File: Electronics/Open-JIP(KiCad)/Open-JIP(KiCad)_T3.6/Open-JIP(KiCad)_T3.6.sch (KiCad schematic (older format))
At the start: 31 parts, among them J1 EJ503A, J2 Screw_Terminal_01x02, U1 74HC4066D,653, U2 74HC4066D,653, U3 KA7812ETU, U4 OPA320AIDBVT, U5 Teensy3.6

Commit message: finished v0.3 for teensy 3.2 and added gerber files
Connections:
- net GNDA: now also C5.2, U4.2 (V-)
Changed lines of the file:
@@
 	1950 5250 1950 5350
 Connection ~ 1950 5350
+Wire Wire Line
+	4300 3800 4300 4100
+Wire Wire Line
+	4300 4100 4450 4100
+Connection ~ 4300 3800
+Connection ~ 4450 4100
 $EndSCHEMATC

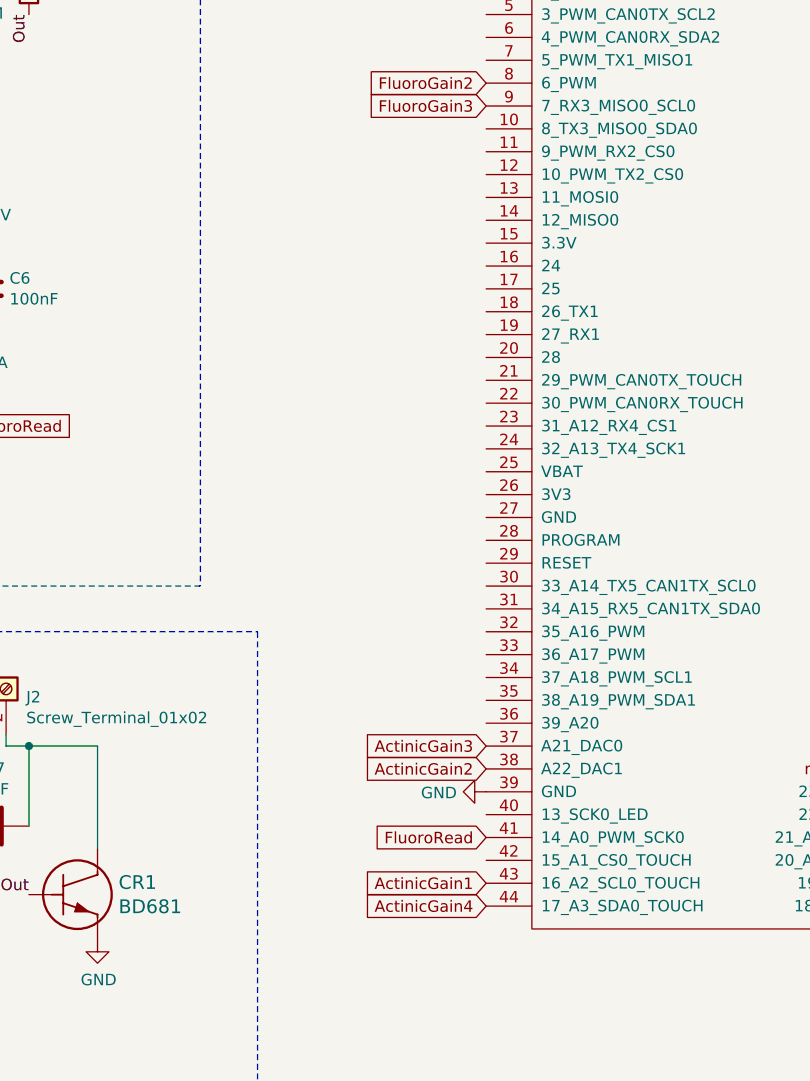
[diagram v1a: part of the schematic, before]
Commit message: added J-step measuring procedure
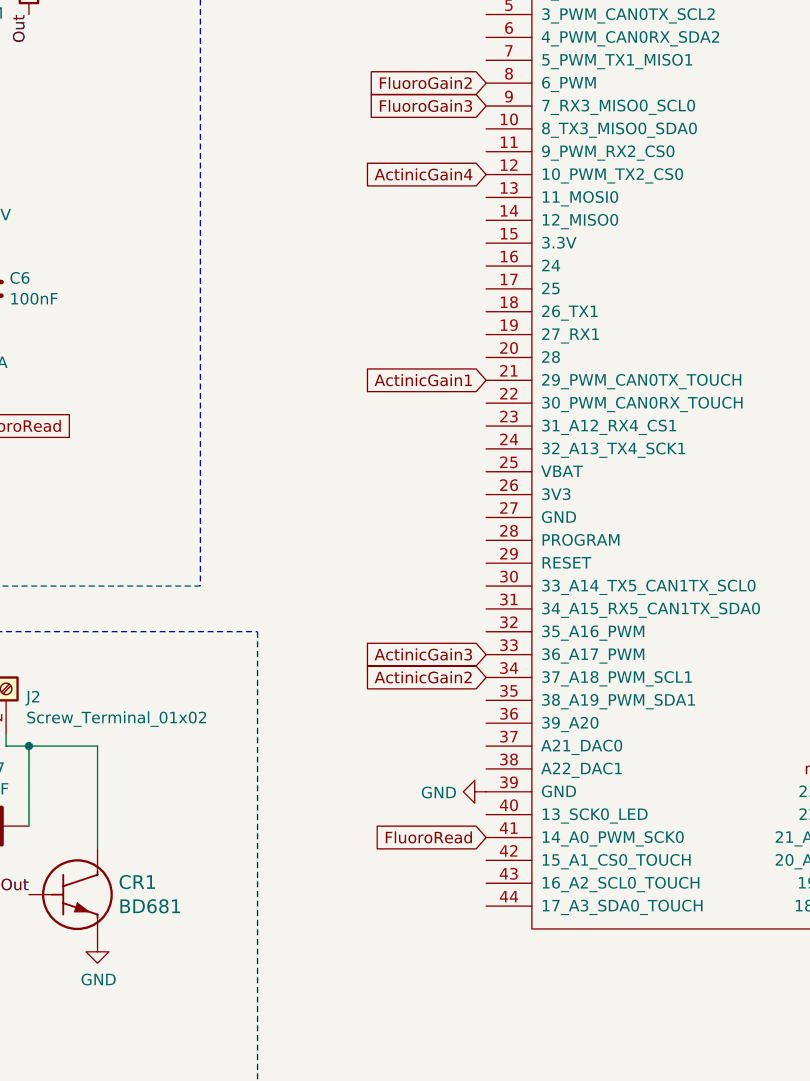
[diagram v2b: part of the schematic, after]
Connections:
- net ActinicGain1: now also U5.21 (29_PWM_CAN0TX_TOUCH); no longer U5.43 (16_A2_SCL0_TOUCH)
- net ActinicGain2: now also U5.34 (37_A18_PWM_SCL1); no longer U5.38 (A22_DAC1)
- net ActinicGain3: now also U5.33 (36_A17_PWM); no longer U5.37 (A21_DAC0)
- net ActinicGain4: now also U5.12 (10_PWM_TX2_CS0); no longer U5.44 (17_A3_SDA0_TOUCH)
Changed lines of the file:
@@
 Text GLabel 2500 6700 0    50   Input ~ 0
 ActinicGain4
-Text GLabel 7200 5700 0    50   Input ~ 0
+Text GLabel 7200 3500 0    50   Input ~ 0
 ActinicGain1
-Text GLabel 7200 5200 0    50   Input ~ 0
+Text GLabel 7200 4800 0    50   Input ~ 0
 ActinicGain2
-Text GLabel 7200 5100 0    50   Input ~ 0
+Text GLabel 7200 4700 0    50   Input ~ 0
 ActinicGain3
-Text GLabel 7200 5800 0    50   Input ~ 0
+Text GLabel 7200 2600 0    50   Input ~ 0
 ActinicGain4
 $Comp

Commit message: update firmware for v0.3
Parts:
- R11: value 4.3K -> 5.1K
- R4: value 8.2K -> 10K
- R6: value 6.8K -> 8.2K
- R8: value 2.3M -> 2M
- R9: value 5.1K -> 6.8K
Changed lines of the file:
@@
 P 4850 1850
 F 0 "R8" H 4780 1804 50  0000 R CNN
-F 1 "2.3M" H 4780 1895 50  0000 R CNN
+F 1 "2M" H 4780 1895 50  0000 R CNN
 F 2 "Resistor_SMD:R_0805_2012Metric_Pad1.20x1.40mm_HandSolder" V 4780 1850 50  0001 C CNN
 F 3 "~" H 4850 1850 50  0001 C CNN
@@
 P 4250 7050
 F 0 "R4" H 4180 7004 50  0000 R CNN
-F 1 "8.2K" H 4180 7095 50  0000 R CNN
+F 1 "10K" H 4180 7095 50  0000 R CNN
 F 2 "Resistor_SMD:R_0805_2012Metric_Pad1.20x1.40mm_HandSolder" V 4180 7050 50  0001 C CNN
 F 3 "~" H 4250 7050 50  0001 C CNN
@@
 P 4950 6850
 F 0 "R9" H 4880 6804 50  0000 R CNN
-F 1 "5.1K" H 4880 6895 50  0000 R CNN
+F 1 "6.8K" H 4880 6895 50  0000 R CNN
 F 2 "Resistor_SMD:R_0805_2012Metric_Pad1.20x1.40mm_HandSolder" V 4880 6850 50  0001 C CNN
 F 3 "~" H 4950 6850 50  0001 C CNN
@@
 P 5300 6750
 F 0 "R11" H 5230 6704 50  0000 R CNN
-F 1 "4.3K" H 5230 6795 50  0000 R CNN
+F 1 "5.1K" H 5230 6795 50  0000 R CNN
 F 2 "Resistor_SMD:R_0805_2012Metric_Pad1.20x1.40mm_HandSolder" V 5230 6750 50  0001 C CNN
 F 3 "~" H 5300 6750 50  0001 C CNN
@@
 P 4600 6950
 F 0 "R6" H 4530 6904 50  0000 R CNN
-F 1 "6.8K" H 4530 6995 50  0000 R CNN
+F 1 "8.2K" H 4530 6995 50  0000 R CNN
 F 2 "Resistor_SMD:R_0805_2012Metric_Pad1.20x1.40mm_HandSolder" V 4530 6950 50  0001 C CNN
 F 3 "~" H 4600 6950 50  0001 C CNN

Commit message: adding optical density to fluorometer
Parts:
- removed U3: KA7812ETU, Additional-parts:TO253P1067X470X2040-3, symbol KA7812ETU:KA7812ETU
- added C? (x2): 100nF, Capacitor_SMD:C_0805_2012Metric_Pad1.18x1.45mm_HandSolder, symbol Open-JIP(KiCad)_T3.6-rescue:C-Device
- added D?: LED, symbol Device:LED
- added Q?: FDN337N, SSOT-3, symbol FDN337N:FDN337N
- added R?: 300, Resistor_SMD:R_0805_2012Metric_Pad1.20x1.40mm_HandSolder, symbol Open-JIP(KiCad)_T3.6-rescue:R-Device
- added R?: 50K, Resistor_SMD:R_0805_2012Metric_Pad1.20x1.40mm_HandSolder, symbol Open-JIP(KiCad)_T3.6-rescue:R-Device
- added R?: 220, Resistor_SMD:R_0805_2012Metric_Pad1.20x1.40mm_HandSolder, symbol Open-JIP(KiCad)_T3.6-rescue:R-Device
- added R?: 10K, Resistor_SMD:R_0805_2012Metric_Pad1.20x1.40mm_HandSolder, symbol Open-JIP(KiCad)_T3.6-rescue:R-Device
- added TP?: 0.001, symbol Connector:TestPoint
- added TP?: OA-Out, symbol Connector:TestPoint
- added TP?: FG1, symbol Connector:TestPoint
- added TP?: FG2, symbol Connector:TestPoint
- added TP?: FG3, symbol Connector:TestPoint
- added TP?: FG4, symbol Connector:TestPoint
- added TP? (x2): AGND, symbol Connector:TestPoint
- added TP?: ODPwr, symbol Connector:TestPoint
- added TP?: 12V, symbol Connector:TestPoint
- added TP?: 6V, symbol Connector:TestPoint
- added U?: OPA320AIDBVT, Additional-parts:SOT95P280X145-5N, symbol Open-JIP(KiCad)_T3.6-rescue:OPA320AIDBVT-OPA320AIDBVT
- added U?: L7806CD2T-TR, symbol VREG_L7806CD2T-TR:L7806CD2T-TR
- C1, C2, C3, C4, C5, C6: symbol Device:C -> Open-JIP(KiCad)_T3.6-rescue:C-Device
- C7: value 1uF -> 0.5uF; symbol Device:C -> Open-JIP(KiCad)_T3.6-rescue:C-Device
- CR1: symbol BD681:BD681 -> Open-JIP(KiCad)_T3.6-rescue:BD681-BD681
- D1: symbol SFH_213_FA:SFH_213_FA -> Open-JIP(KiCad)_T3.6-rescue:SFH_213_FA-SFH_213_FA
- D2, D3: symbol Device:LED -> Open-JIP(KiCad)_T3.6-rescue:LED-Device
- J1: symbol DCJack_EJ503A:EJ503A -> Open-JIP(KiCad)_T3.6-rescue:EJ503A-DCJack_EJ503A
- J2: symbol Connector:Screw_Terminal_01x02 -> Open-JIP(KiCad)_T3.6-rescue:Screw_Terminal_01x02-Connector
- R1, R11, R12, R13, R2, R4, R6, R7, R9: symbol Device:R -> Open-JIP(KiCad)_T3.6-rescue:R-Device
- R10: value 1M -> 100K; symbol Device:R -> Open-JIP(KiCad)_T3.6-rescue:R-Device
- R3: value 3.9M -> 10K; symbol Device:R -> Open-JIP(KiCad)_T3.6-rescue:R-Device
- R5: value 3.3M -> 20K; symbol Device:R -> Open-JIP(KiCad)_T3.6-rescue:R-Device
- R8: value 2M -> 50K; symbol Device:R -> Open-JIP(KiCad)_T3.6-rescue:R-Device
- U1, U2: symbol 74HC4066D_653:74HC4066D,653 -> Open-JIP(KiCad)_T3.6-rescue:74HC4066D,653-74HC4066D_653
- U4: symbol OPA320AIDBVT:OPA320AIDBVT -> Open-JIP(KiCad)_T3.6-rescue:OPA320AIDBVT-OPA320AIDBVT
- U5: symbol teensy:Teensy3.6 -> Open-JIP(KiCad)_T3.6-rescue:Teensy3.6-teensy
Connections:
- net +15V: no longer C2.2, J1.1
- net +3V3: now also C?.2, U?.5 (V+)
- net +5V: now also R?.2
- net FluoroGain1: now also TP?.1
- net FluoroGain2: now also TP?.1
- net FluoroGain3: now also TP?.1
- net FluoroGain4: now also TP?.1
- net GND: now also Q?.2, R?.1, U?.3 (GND)
- net GNDA: now also C?.1, C?.1, C?.2, R?.1, TP?.1, TP?.1, U?.2 (V-)
- net Out: now also U?.3 (+IN); no longer R7.2
- net ODEmitter: now reaches U5.47 (20_A6_PWM_CS0_SCK1)
- net ODEmitter: now also Q?.1, R?.2, TP?.1
- net at C1.2, R1.1, R2.2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: now also TP?.1
- net at C4.2, C7.1, J2.1 (Pin_1): now also TP?.1, U?.2 (Output)
- new net: R7.2, R?.1, TP?.1, U?.1 (OUT)
- new net: C2.2, J1.1, TP?.1, U?.1 (Input)
- new net: R?.2, R?.2, U?.4 (-IN)
- new net: D?.1 (K), Q?.3
- new net: D?.2 (A), R?.1
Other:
- note added: "Open-JIP v0.4\n"
- note added: "Optical Density Emitter"
- note removed: "Open-JIP v0.3"
- moved on the sheet: C2, C4, C6, C7, CR1, D2, D3, J1, J2, R11, R12, R13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

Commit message: od and fluorometer design
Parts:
- removed C5, C6, C?: 100nF, Capacitor_SMD:C_0805_2012Metric_Pad1.18x1.45mm_HandSolder, symbol Open-JIP(KiCad)_T3.6-rescue:C-Device
- removed TP?: FG1, symbol Connector:TestPoint
- removed TP?: FG2, symbol Connector:TestPoint
- removed TP?: FG3, symbol Connector:TestPoint
- removed TP?: FG4, symbol Connector:TestPoint
- removed TP? (x2): AGND, symbol Connector:TestPoint
- removed TP?: ODPwr, symbol Connector:TestPoint
- removed TP?: 12V, symbol Connector:TestPoint
- removed TP?: 6V, symbol Connector:TestPoint
- added J1, J4: B3B-PH-SM4-TB(LF)(SN), JST_B3B-PH-SM4-TB(LF)(SN), symbol B3B-PH-SM4-TB_LF__SN_:B3B-PH-SM4-TB(LF)(SN)
- added TP1: GND1, TestPoint:TestPoint_Pad_D1.5mm, symbol Connector:TestPoint
- added TP2: 5VA, TestPoint:TestPoint_Pad_D1.5mm, symbol Connector:TestPoint
- added TP4: TrigOut, TestPoint:TestPoint_Pad_D1.5mm, symbol Connector:TestPoint
- D1: renamed from D?; footprint (none) -> LED_SMD:LED_1206_3216Metric_Pad1.42x1.75mm_HandSolder
- Q1: renamed from Q?; footprint SSOT-3 -> Additional-parts:SSOT-3
- TP3, TP5: renamed from TP?; footprint (none) -> TestPoint:TestPoint_Pad_D1.5mm
- U1: renamed from U?; footprint (none) -> Additional-parts:VREG_L7805CDT-TR
- gave numbers to parts that had none: 6
- renumbered C7 to C5, D1 to D2, D2 to D3, D3 to D4, J1 to J2, J2 to J3, R9 to R10, R10 to R11, R11 to R13, R7 to R15, R12 to R16, R13 to R17, R1 to R2, R2 to R3, R3 to R5, R4 to R6, R5 to R7, R6 to R8, R8 to R9, U1 to U2, U2 to U3, U5 to U6
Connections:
- net +15V is gone; now on net +12V: R17.1
- net +3V3: now also U6.15 (3.3V)
- net +5V: now also J4.2; no longer R4.2
- net ActinicGain1: now also U6.43 (16_A2_SCL0_TOUCH); no longer U6.21 (29_PWM_CAN0TX_TOUCH)
- net ActinicGain2: now also U6.35 (38_A19_PWM_SDA1); no longer U6.34 (37_A18_PWM_SCL1)
- net ActinicGain3: now also U6.34 (37_A18_PWM_SCL1); no longer U6.33 (36_A17_PWM)
- net ActinicGain4: now also U6.44 (17_A3_SDA0_TOUCH); no longer U6.12 (10_PWM_TX2_CS0)
- net FluoroRead: now also TP5.1
- net GND: now also U6.1 (GND), J4.1; no longer Q1.2, R1.1
- net ODEmitter: now also J4.3; no longer Q1.1, R1.2
- net at C5.2, CR1.2 (C), J3.2 (Pin_2): now also TP4.1
- net at R14.1, R15.2, U5.1 (OUT): no longer TP5.1
- net +12V: now reaches C2.2, J2.1, U1.1 (Input)
- new net +5VA: J1.2, R4.2, TP2.1
- new net GND1: J1.1, Q1.2, R1.1, TP1.1
- new net ODEmitter1: J1.3, Q1.1, R1.2
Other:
- moved on the sheet: D1, Q1, R1, R4, TP5

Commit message: refactored electronics desgin
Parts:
- removed C1, C4, C6: 100nF, Capacitor_SMD:C_0805_2012Metric_Pad1.18x1.45mm_HandSolder, symbol Open-JIP(KiCad)_T3.6-rescue:C-Device
- removed C2: 330nF, Capacitor_SMD:C_0805_2012Metric_Pad1.18x1.45mm_HandSolder, symbol Open-JIP(KiCad)_T3.6-rescue:C-Device
- removed C3: 1pF, Capacitor_SMD:C_0805_2012Metric_Pad1.18x1.45mm_HandSolder, symbol Open-JIP(KiCad)_T3.6-rescue:C-Device
- removed C5: 0.5uF, Capacitor_SMD:CP_Elec_4x5.4, symbol Open-JIP(KiCad)_T3.6-rescue:C-Device
- removed CR1: BD681, Additional-parts:BD681, symbol Open-JIP(KiCad)_T3.6-rescue:BD681-BD681
- removed D1: LED, LED_SMD:LED_1206_3216Metric_Pad1.42x1.75mm_HandSolder, symbol Device:LED
- removed D2: SFH_213_FA, Additional-parts:SFH_213_FA, symbol Open-JIP(KiCad)_T3.6-rescue:SFH_213_FA-SFH_213_FA
- removed D3, D4: LED, LED_SMD:LED_0805_2012Metric_Pad1.15x1.40mm_HandSolder, symbol Open-JIP(KiCad)_T3.6-rescue:LED-Device
- removed J2: EJ503A, Additional-parts:DCJack_MPD_EJ503A, symbol Open-JIP(KiCad)_T3.6-rescue:EJ503A-DCJack_EJ503A
- removed J3: Screw_Terminal_01x02, TerminalBlock:TerminalBlock_Altech_AK300-2_P5.00mm, symbol Open-JIP(KiCad)_T3.6-rescue:Screw_Terminal_01x02-Connector
- removed R1, R5, R6: 10K, Resistor_SMD:R_0805_2012Metric_Pad1.20x1.40mm_HandSolder, symbol Open-JIP(KiCad)_T3.6-rescue:R-Device
- removed R10: 6.8K, Resistor_SMD:R_0805_2012Metric_Pad1.20x1.40mm_HandSolder, symbol Open-JIP(KiCad)_T3.6-rescue:R-Device
- removed R11: 100K, Resistor_SMD:R_0805_2012Metric_Pad1.20x1.40mm_HandSolder, symbol Open-JIP(KiCad)_T3.6-rescue:R-Device
- removed R12: 300, Resistor_SMD:R_0805_2012Metric_Pad1.20x1.40mm_HandSolder, symbol Open-JIP(KiCad)_T3.6-rescue:R-Device
- removed R13: 5.1K, Resistor_SMD:R_0805_2012Metric_Pad1.20x1.40mm_HandSolder, symbol Open-JIP(KiCad)_T3.6-rescue:R-Device
- removed R14, R9: 50K, Resistor_SMD:R_0805_2012Metric_Pad1.20x1.40mm_HandSolder, symbol Open-JIP(KiCad)_T3.6-rescue:R-Device
- removed R15: 47, Resistor_SMD:R_0805_2012Metric_Pad1.20x1.40mm_HandSolder, symbol Open-JIP(KiCad)_T3.6-rescue:R-Device
- removed R16: 1K, Resistor_SMD:R_0805_2012Metric_Pad1.20x1.40mm_HandSolder, symbol Open-JIP(KiCad)_T3.6-rescue:R-Device
- removed R17: 15K, Resistor_SMD:R_0805_2012Metric_Pad1.20x1.40mm_HandSolder, symbol Open-JIP(KiCad)_T3.6-rescue:R-Device
- removed R2, R7: 20K, Resistor_SMD:R_0805_2012Metric_Pad1.20x1.40mm_HandSolder, symbol Open-JIP(KiCad)_T3.6-rescue:R-Device
- removed R3: 5, Resistor_SMD:R_0805_2012Metric_Pad1.20x1.40mm_HandSolder, symbol Open-JIP(KiCad)_T3.6-rescue:R-Device
- removed R4: 220, Resistor_SMD:R_0805_2012Metric_Pad1.20x1.40mm_HandSolder, symbol Open-JIP(KiCad)_T3.6-rescue:R-Device
- removed R8: 8.2K, Resistor_SMD:R_0805_2012Metric_Pad1.20x1.40mm_HandSolder, symbol Open-JIP(KiCad)_T3.6-rescue:R-Device
- removed TP1: GND1, TestPoint:TestPoint_Pad_D1.5mm, symbol Connector:TestPoint
- removed TP2: 5VA, TestPoint:TestPoint_Pad_D1.5mm, symbol Connector:TestPoint
- removed TP3: 0.001, TestPoint:TestPoint_Pad_D1.5mm, symbol Connector:TestPoint
- removed TP4: TrigOut, TestPoint:TestPoint_Pad_D1.5mm, symbol Connector:TestPoint
- removed TP5: OA-Out, TestPoint:TestPoint_Pad_D1.5mm, symbol Connector:TestPoint
- removed U2, U3: 74HC4066D,653, Additional-parts:SOIC127P600X175-14N, symbol Open-JIP(KiCad)_T3.6-rescue:74HC4066D,653-74HC4066D_653
- removed U4, U5: OPA320AIDBVT, Additional-parts:SOT95P280X145-5N, symbol Open-JIP(KiCad)_T3.6-rescue:OPA320AIDBVT-OPA320AIDBVT
- removed U6: Teensy3.6, Teensy:Teensy35_36, symbol Open-JIP(KiCad)_T3.6-rescue:Teensy3.6-teensy
- added C?: 330, symbol Device:C
- added C? (x3): 100nF, symbol Device:C
- added C?: 0.5uF, symbol Device:C
- added C?: 1pF, symbol Device:C
- added CR?: BD681, SOT-32_STM, symbol BD681:BD681
- added D? (x3): LED, symbol Device:LED
- added D?: SFH_213_FA, XDCR_SFH_213_FA, symbol SFH_213_FA:SFH_213_FA
- added J?: EJ503A, MPD_EJ503A, symbol DCJack_EJ503A:EJ503A
- added J?: Screw_Terminal_01x02, symbol Connector:Screw_Terminal_01x02
- added R?: 10K, symbol Device:R
- added R?: 220, symbol Device:R
- added R? (x8): R, symbol Device:R
- added R?: 300, symbol Device:R
- added R?: 5, symbol Device:R
- added R?: 20K, symbol Device:R
- added R?: 47, symbol Device:R
- added R?: 150K, symbol Device:R
- added R?: 1K, symbol Device:R
- added R?: 15K, symbol Device:R
- added TP?: GND1, symbol Connector:TestPoint
- added TP?: TriggOut, symbol Connector:TestPoint
- added TP?: OAout, symbol Connector:TestPoint
- added U? (x2): 74HC4066D,653, SOIC127P600X175-14N, symbol 74HC4066D_653:74HC4066D,653
- added U? (x2): OPA320AIDBVR, SOT95P280X145-5N, symbol OPA320AIDBVR:OPA320AIDBVR
- added U?: Teensy3.6, symbol teensy:Teensy3.6
